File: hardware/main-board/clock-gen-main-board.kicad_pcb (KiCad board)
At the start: 2 copper layers, 55 x 55 mm, 10 parts, among them J1 Conn_01x03_Pin, J2 Conn_01x03_Pin, J3 Conn_01x03_Pin, U1 Pico

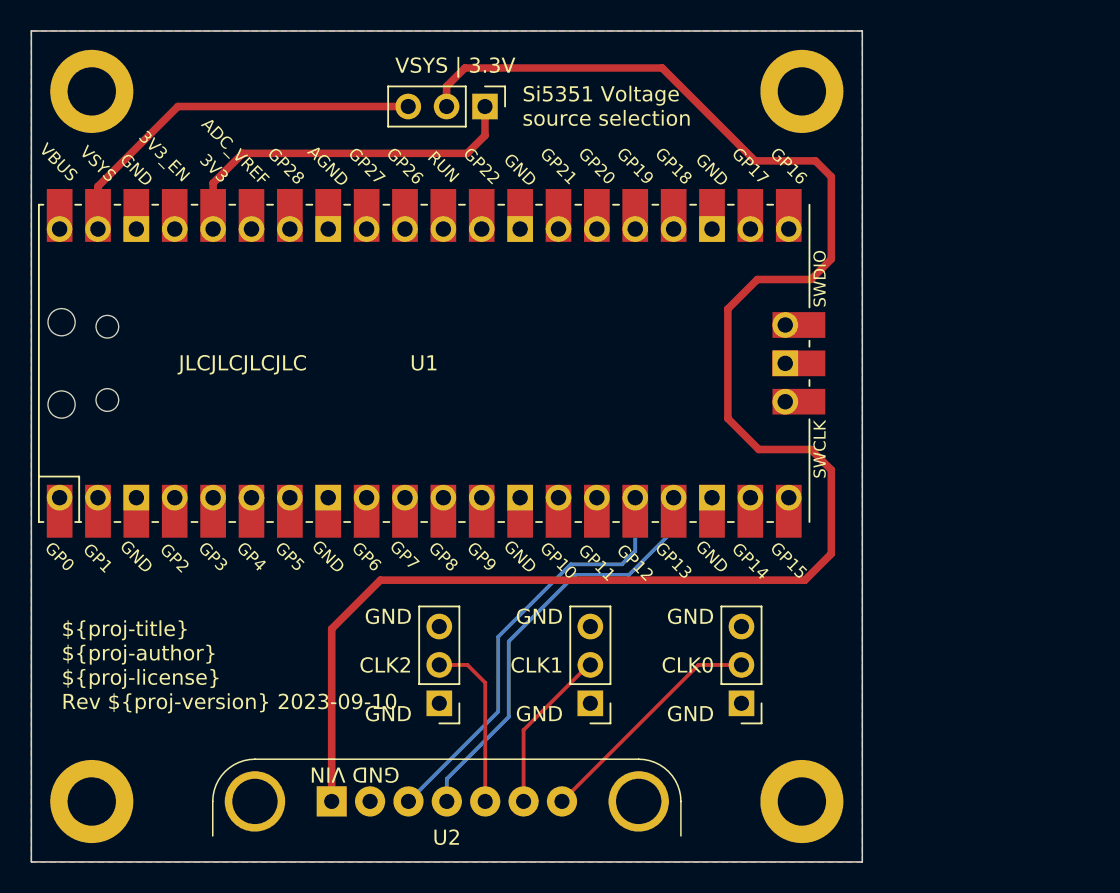
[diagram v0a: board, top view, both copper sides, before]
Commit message: Resolve "Extend mainboard with audio ADC"
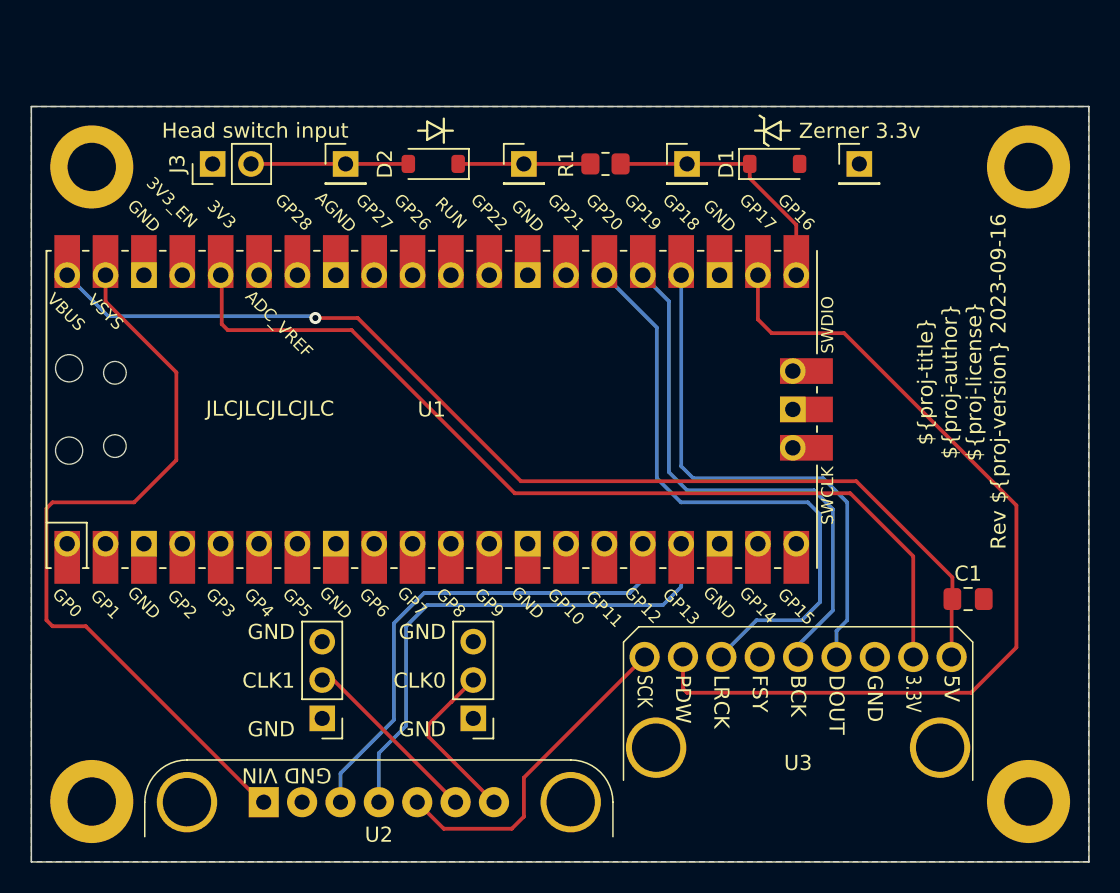
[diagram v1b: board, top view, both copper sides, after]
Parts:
- removed JP1: Jumper_3_Bridged12, Connector_PinHeader_2.54mm:PinHeader_1x03_P2.54mm_Vertical
- added C1: 10u, Capacitor_SMD:C_0805_2012Metric_Pad1.18x1.45mm_HandSolder, F.Cu at (160.0, 112.6)
- added D1: D_Zener, Diode_SMD:D_SOD-123, F.Cu at (147.2, 83.8)
- added D2: D, Diode_SMD:D_SOD-123, F.Cu at (124.6, 83.8)
- added J4: Conn_01x01_Pin, Connector_PinHeader_2.54mm:PinHeader_1x01_P2.54mm_Vertical, F.Cu at (141.4, 83.8)
- added J5: Conn_01x01_Pin, Connector_PinHeader_2.54mm:PinHeader_1x01_P2.54mm_Vertical, F.Cu at (152.8, 83.8)
- added J6: Conn_01x01_Pin, Connector_PinHeader_2.54mm:PinHeader_1x01_P2.54mm_Vertical, F.Cu at (118.8, 83.8)
- added J7: Conn_01x01_Pin, Connector_PinHeader_2.54mm:PinHeader_1x01_P2.54mm_Vertical, F.Cu at (130.6, 83.8)
- added R1: 1k, Resistor_SMD:R_0805_2012Metric_Pad1.20x1.40mm_HandSolder, F.Cu at (136.0, 83.8)
- added U3: ~, black-pcm1802:black-pcm1802-board, F.Cu at (148.8, 114.4)
- J3: value Conn_01x03_Pin -> Conn_01x02_Pin; footprint Connector_PinHeader_2.54mm:PinHeader_1x03_P2.54mm_Vertical -> Connector_PinHeader_2.54mm:PinHeader_1x02_P2.54mm_Vertical
- moved J3 38.7 mm to (110.0, 83.8), turned to 90 degrees
- moved J1 17.8 mm to (127.2, 120.5)
- moved J2 17.8 mm to (117.2, 120.5)
- moved H2 15.8 mm to (164.0, 84.0)
- moved H3 15.0 mm to (164.0, 126.0)
- moved H1 5.00 mm to (102.0, 84.0)
- moved U2 4.50 mm to (121.0, 123.2)
- moved U1 3.09 mm to (124.5, 100.0)
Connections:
- net /SCL renamed /Gen.SCL
- net /SDA renamed /Gen.SDA
- J3 pad 2: Net-(J3-Pin_2) -> Net-(D2-A)
- U1 pad 21: unconnected-(U1-GPIO16-Pad21) -> Net-(D1-K)
- U1 pad 22: unconnected-(U1-GPIO17-Pad22) -> /PCM.PwrDn
- U1 pad 24: unconnected-(U1-GPIO18-Pad24) -> /PCM.Data
- U1 pad 25: unconnected-(U1-GPIO19-Pad25) -> /PCM.BitClk
- U1 pad 26: unconnected-(U1-GPIO20-Pad26) -> /PCM.LRClk
- U1 pad 36: Net-(JP1-A) -> /PCM.3V3
- U1 pad 39: Net-(JP1-B) -> /Gen.VSI
- U1 pad 40: unconnected-(U1-VBUS-Pad40) -> /PCM.5V
- U2 pad 3: Net-(J3-Pin_2) -> /PCM.SysClk
- U2 pad 7: /VSI -> /Gen.VSI
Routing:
- net /VSI: track 111.6 -> 0.00 mm
- net /PCM.5V: track 0.00 -> 72.2 mm, vias 0 -> 1
- net /PCM.3V3: track 0.00 -> 62.1 mm
- net /PCM.PwrDn: track 0.00 -> 60.1 mm
- net /Gen.VSI: track 0.00 -> 50.9 mm
- net /PCM.LRClk: track 0.00 -> 40.6 mm
- net /PCM.BitClk: track 0.00 -> 36.4 mm
- net /PCM.Data: track 0.00 -> 35.2 mm
- net Net-(JP1-B): track 25.5 -> 0.00 mm
- net Net-(JP1-A): track 24.3 -> 0.00 mm
- net /PCM.SysClk: track 0.00 -> 22.0 mm
- net Net-(D1-K): track 0.00 -> 17.2 mm
- net Net-(J3-Pin_2): track 11.4 -> 0.00 mm
- net Net-(D2-A): track 0.00 -> 10.4 mm
- net Net-(D2-K): track 0.00 -> 8.75 mm
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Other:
- board size 55 x 55 mm -> 70 x 50 mm
- board text added: "3.8mm"
- board text added: "31.7mm"
- board text added: "37.4mm"
- board text added: "42mm"
- board text added: "50mm"
- board text added: "56.2mm"
- board text added: "6.3mm"
- board text added: "62.0mm"
- board text added: "70mm"
- board text added: "Head switch input"
- board text added: "Zerner 3.3v"
- board text removed: "47mm"
- board text removed: "55mm"
- board text removed: "GND CLK2 GND"
- board text removed: "Si5351 Voltage source selection"
- board text removed: "VSYS | 3.3V"
